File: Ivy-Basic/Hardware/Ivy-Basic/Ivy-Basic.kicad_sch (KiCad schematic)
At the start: 2 parts, among them U1 ESP32-S3-MINI-1, U2 TMC2208-LA

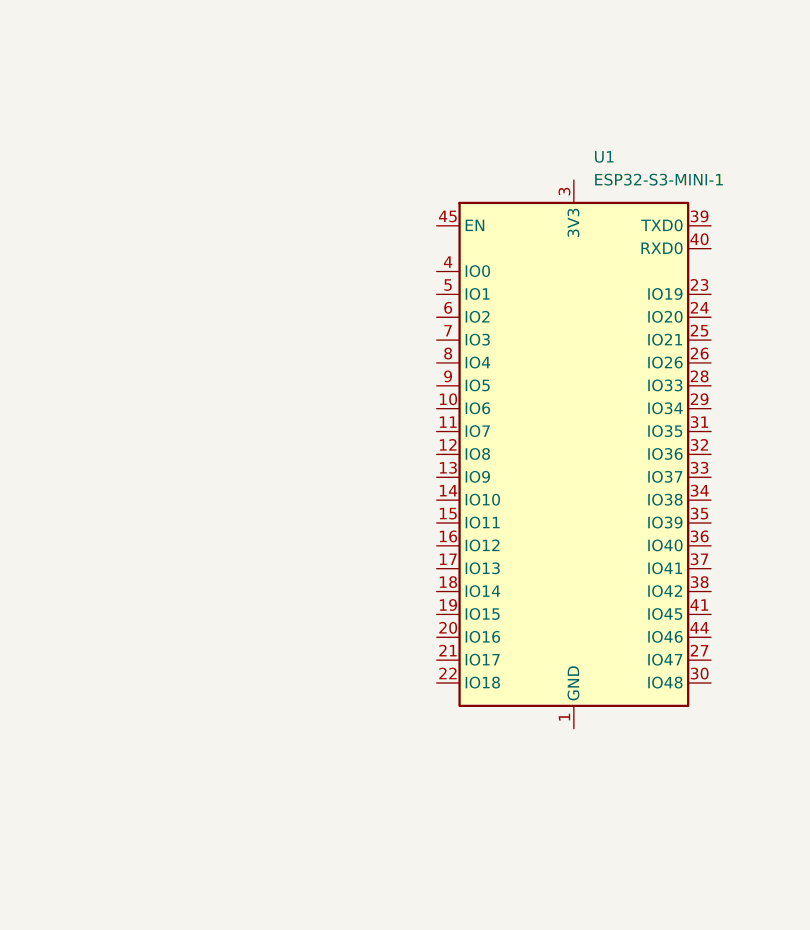
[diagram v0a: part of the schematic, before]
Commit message: add switching buck converter
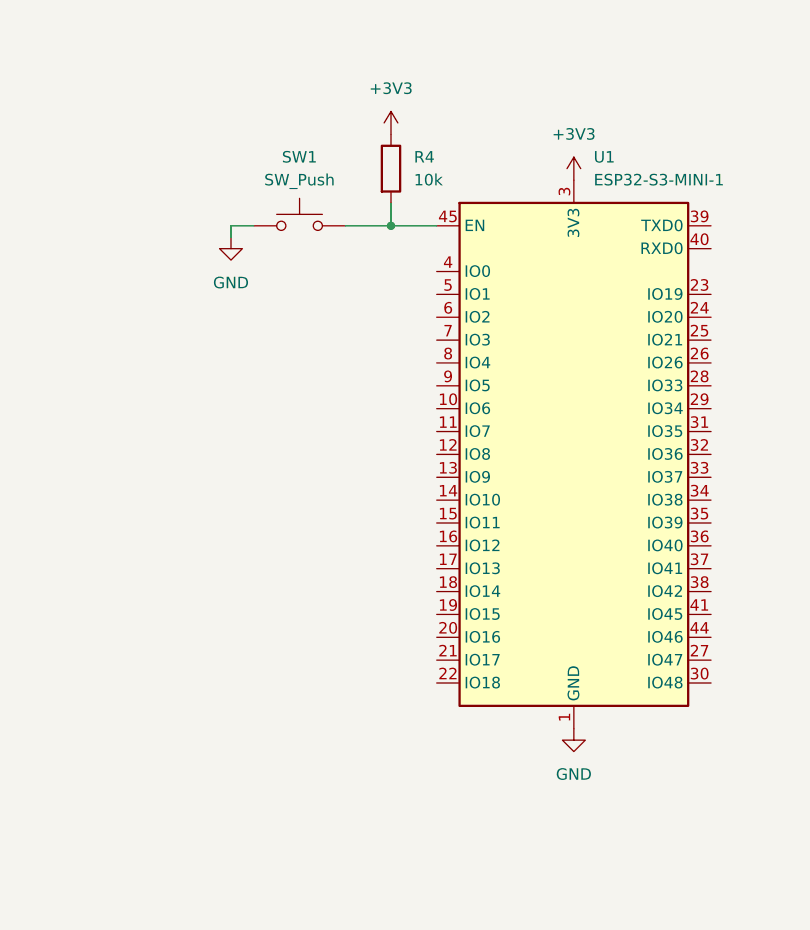
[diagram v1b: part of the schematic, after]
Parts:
- added R4: 10k, symbol Device:R
- added SW1: SW_Push, symbol Switch:SW_Push
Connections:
- net GND: now reaches U1.1 (GND), U1.2 (GND), U1.42 (GND), U1.43 (GND), U1.46 (GND), U1.47 (GND), U1.48 (GND), U1.49 (GND), U1.50 (GND), U1.51 (GND), U1.52 (GND), U1.53 (GND), U1.54 (GND), U1.55 (GND), U1.56 (GND), U1.57 (GND), U1.58 (GND), U1.59 (GND), U1.60 (GND), U1.61 (GND), U1.62 (GND), U1.63 (GND), U1.64 (GND), U1.65 (GND)
- net GND: now also SW1.1
- net +3V3: now reaches U1.3 (3V3)
- net +3V3: now also R4.1
- net at U1.45 (EN): now also R4.2, SW1.2

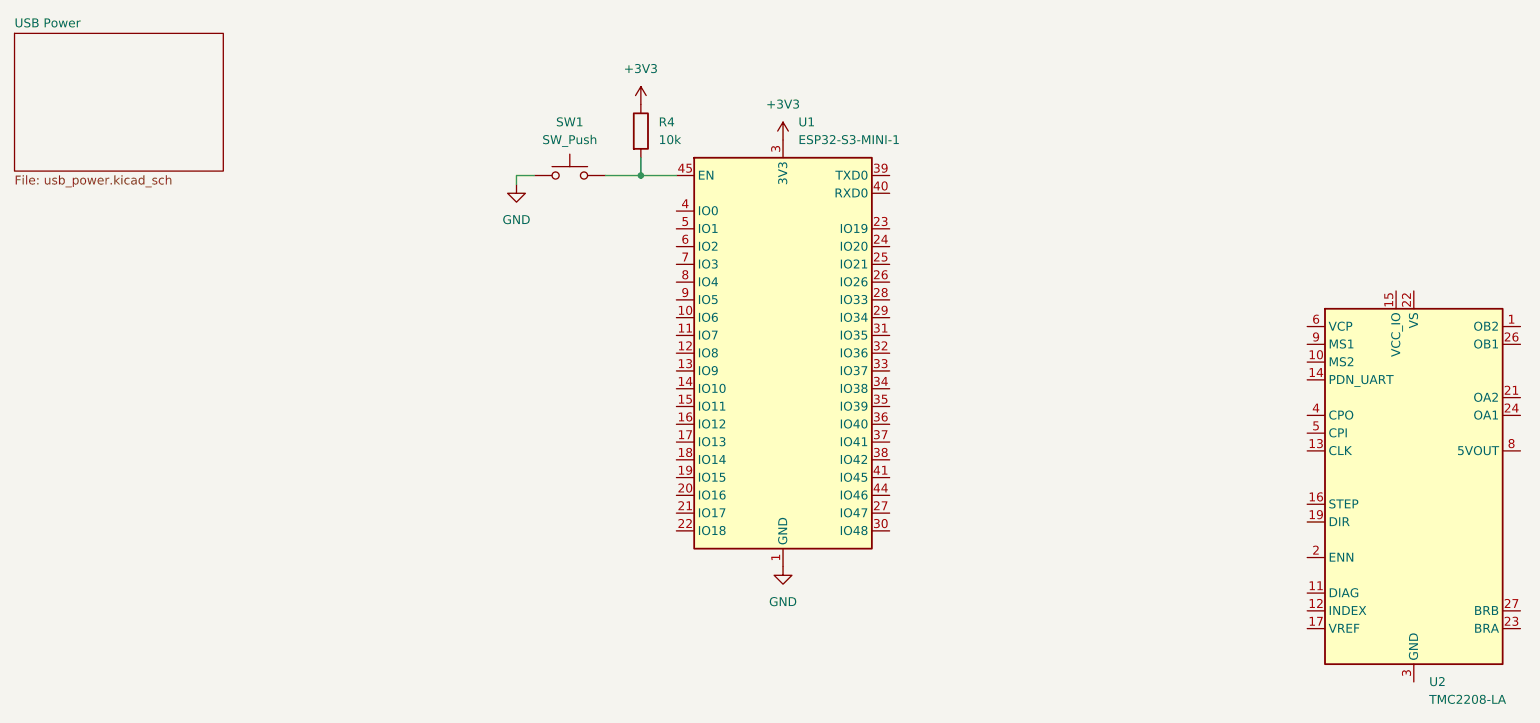
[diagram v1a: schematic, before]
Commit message: add startup rc circuit to esp32
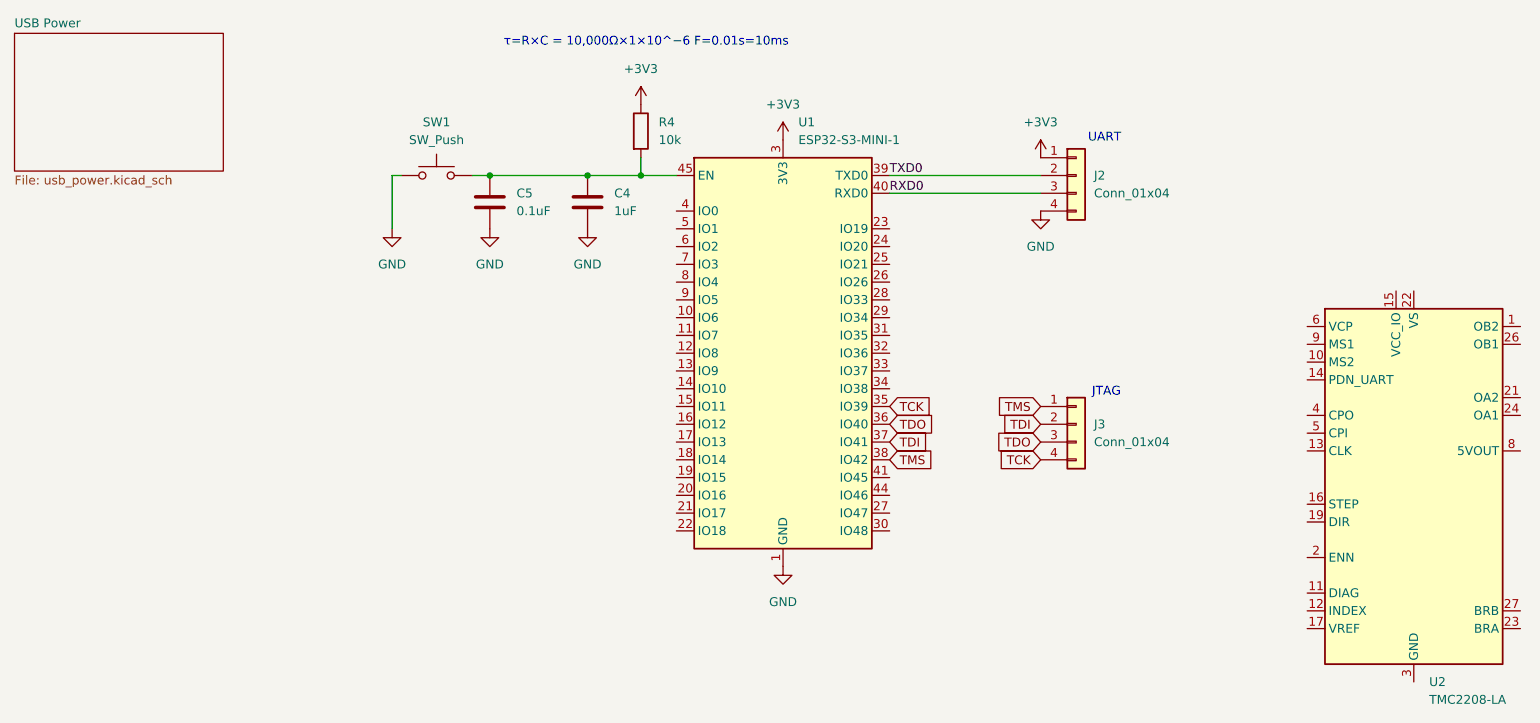
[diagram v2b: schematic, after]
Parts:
- added C4: 1uF, symbol Device:C
- added C5: 0.1uF, symbol Device:C
- added J2, J3: Conn_01x04, symbol Connector_Generic:Conn_01x04
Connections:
- net +3V3: now also J2.1 (Pin_1)
- net GND: now also C4.2, C5.2, J2.4 (Pin_4)
- net at R4.2, SW1.2, U1.45 (EN): now also C4.1, C5.1
- net TCK: now reaches U1.35 (IO39)
- net TCK: now also J3.4 (Pin_4)
- net TDO: now reaches U1.36 (IO40)
- net TDO: now also J3.3 (Pin_3)
- net TDI: now reaches U1.37 (IO41)
- net TDI: now also J3.2 (Pin_2)
- net TMS: now reaches U1.38 (IO42)
- net TMS: now also J3.1 (Pin_1)
- net TXD0: now reaches U1.39 (TXD0)
- net TXD0: now also J2.2 (Pin_2)
- net RXD0: now reaches U1.40 (RXD0)
- net RXD0: now also J2.3 (Pin_3)
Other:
- note added: "JTAG"
- note added: "UART"
- note added: "τ=R×C = 10,000Ω×1×10^−6 F=0.01s=10ms"
- moved on the sheet: SW1
